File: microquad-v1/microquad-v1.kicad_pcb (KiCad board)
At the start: 2 copper layers, 163.8 x 79.1 mm, 79 parts, among them J1 USB_microB_2040002-1, M1 Motor_DC, M2 Motor_DC, M3 Motor_DC, M4 Motor_DC, M5 Motor_DC, M6 Motor_DC, Q1 Q_NMOS_GSD, Q2 Q_NMOS_GSD, Q3 Q_NMOS_GSD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

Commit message: Merged new netlist
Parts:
- Uimu1: footprint QFN40P300X300X105-25N -> imulogger2:QFN40P300X300X105-25N
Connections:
- C5 pad 2: /Motor6/VBAT -> /Motor1/VBAT
- C6 pad 2: /Motor6/VBAT -> /Motor2/VBAT
- C7 pad 2: /Motor6/VBAT -> /Motor3/VBAT
- C8 pad 2: /Motor6/VBAT -> /Motor4/VBAT
- C9 pad 2: /Motor6/VBAT -> /Motor5/VBAT
- D10 pad 1: Net-(D15-Pad2) -> Net-(D10-Pad1)
- D11 pad 1: /Motor6/VBAT -> /Motor4/VBAT
- D11 pad 2: Net-(D15-Pad2) -> Net-(D11-Pad2)
- D12 pad 1: Net-(D15-Pad2) -> Net-(D11-Pad2)
- D13 pad 1: /Motor6/VBAT -> /Motor5/VBAT
- D13 pad 2: Net-(D15-Pad2) -> Net-(D13-Pad2)
- D14 pad 1: Net-(D15-Pad2) -> Net-(D13-Pad2)
- D5 pad 1: /Motor6/VBAT -> /Motor1/VBAT
- D5 pad 2: Net-(D15-Pad2) -> Net-(D5-Pad2)
- D6 pad 1: Net-(D15-Pad2) -> Net-(D5-Pad2)
- D7 pad 1: /Motor6/VBAT -> /Motor2/VBAT
- D7 pad 2: Net-(D15-Pad2) -> Net-(D7-Pad2)
- D8 pad 1: Net-(D15-Pad2) -> Net-(D7-Pad2)
- D9 pad 1: /Motor6/VBAT -> /Motor3/VBAT
- D9 pad 2: Net-(D15-Pad2) -> Net-(D10-Pad1)
- M1 pad 1: /Motor6/VBAT -> /Motor1/VBAT
- M1 pad 2: Net-(D15-Pad2) -> Net-(D5-Pad2)
- M2 pad 1: /Motor6/VBAT -> /Motor2/VBAT
- M2 pad 2: Net-(D15-Pad2) -> Net-(D7-Pad2)
- M3 pad 1: /Motor6/VBAT -> /Motor3/VBAT
- M3 pad 2: Net-(D15-Pad2) -> Net-(D10-Pad1)
- M4 pad 1: /Motor6/VBAT -> /Motor4/VBAT
- M4 pad 2: Net-(D15-Pad2) -> Net-(D11-Pad2)
- M5 pad 1: /Motor6/VBAT -> /Motor5/VBAT
- M5 pad 2: Net-(D15-Pad2) -> Net-(D13-Pad2)
- Q1 pad 1: /Motor6/ENABLE -> /Motor1/ENABLE
- Q1 pad 3: Net-(D15-Pad2) -> Net-(D5-Pad2)
- Q2 pad 1: /Motor6/ENABLE -> /Motor2/ENABLE
- Q2 pad 3: Net-(D15-Pad2) -> Net-(D7-Pad2)
- Q3 pad 1: /Motor6/ENABLE -> /Motor3/ENABLE
- Q3 pad 3: Net-(D15-Pad2) -> Net-(D10-Pad1)
- Q4 pad 1: /Motor6/ENABLE -> /Motor4/ENABLE
- Q4 pad 3: Net-(D15-Pad2) -> Net-(D11-Pad2)
- Q5 pad 1: /Motor6/ENABLE -> /Motor5/ENABLE
- Q5 pad 3: Net-(D15-Pad2) -> Net-(D13-Pad2)

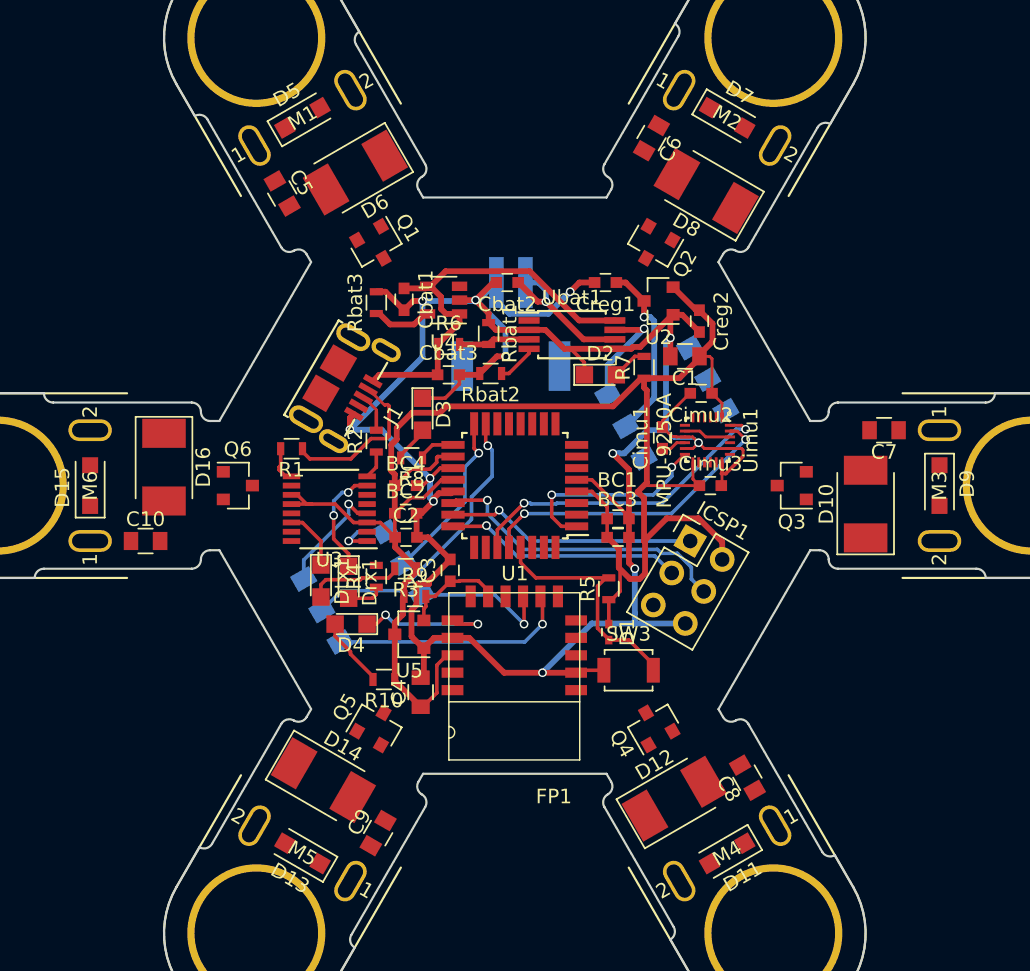
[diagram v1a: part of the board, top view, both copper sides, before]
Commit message: Add tracks on arms and connect VBAT, requires DRC violations... (not actual violations, KiCad just thinks they are)
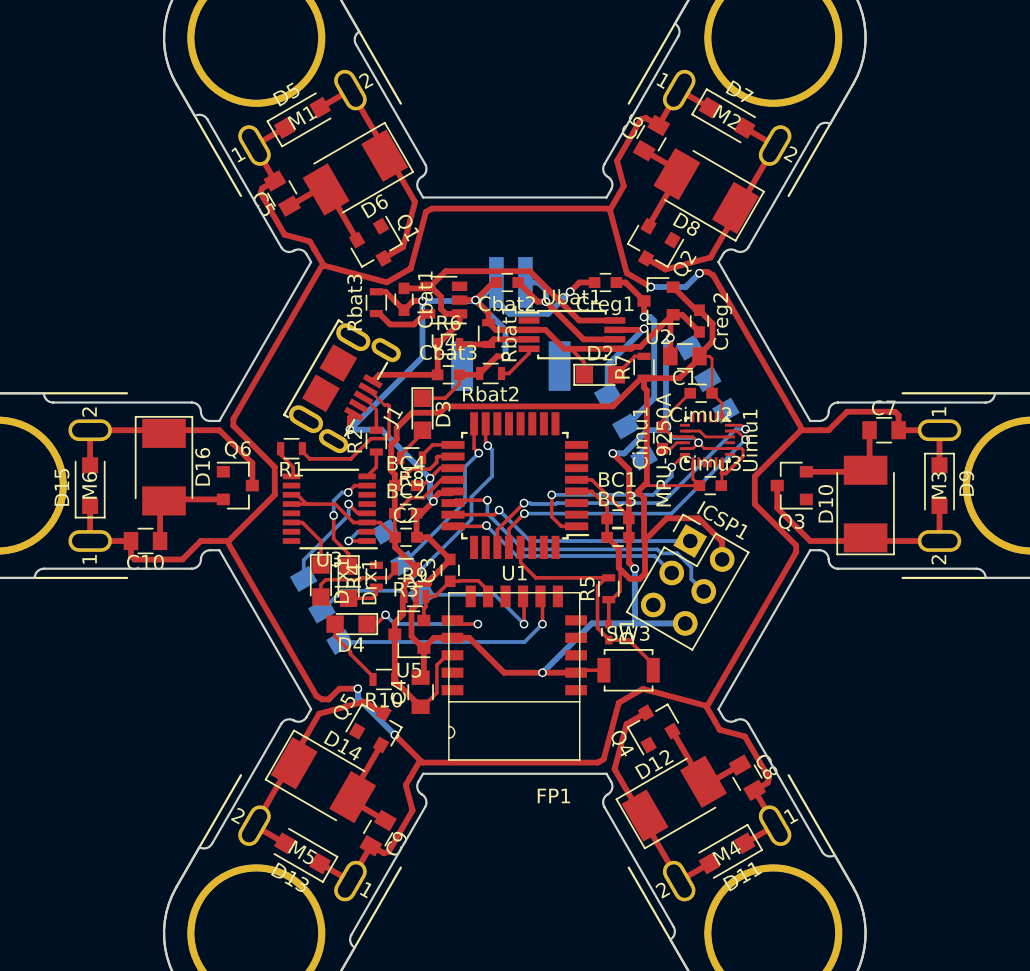
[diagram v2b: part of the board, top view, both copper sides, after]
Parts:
- turned C10 to 180 degrees
- turned C5 to 120 degrees
- turned C6 to 60 degrees
- turned C7 to 0 degrees
- turned C8 to 300 degrees
- turned C9 to 240 degrees
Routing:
- net /Motor4/VBAT: track 0.00 -> 58.9 mm, vias 0 -> 2
- net GND: track 170.6 -> 209.9 mm
- net /Motor2/VBAT: track 0.00 -> 36.8 mm, vias 0 -> 2
- net /Motor6/VBAT: track 0.00 -> 36.7 mm
- net /Motor1/VBAT: track 0.00 -> 36.5 mm
- net /Motor3/VBAT: track 0.00 -> 36.5 mm
- net Net-(D15-Pad2): track 0.00 -> 16.4 mm
- net /Motor5/VBAT: track 0.00 -> 13.6 mm
- net Net-(D7-Pad2): track 0.00 -> 13.5 mm
- net Net-(D13-Pad2): track 0.00 -> 13.5 mm
- net Net-(D10-Pad1): track 0.00 -> 13.5 mm
- net Net-(D5-Pad2): track 0.00 -> 13.5 mm
- net Net-(D11-Pad2): track 0.00 -> 13.5 mm

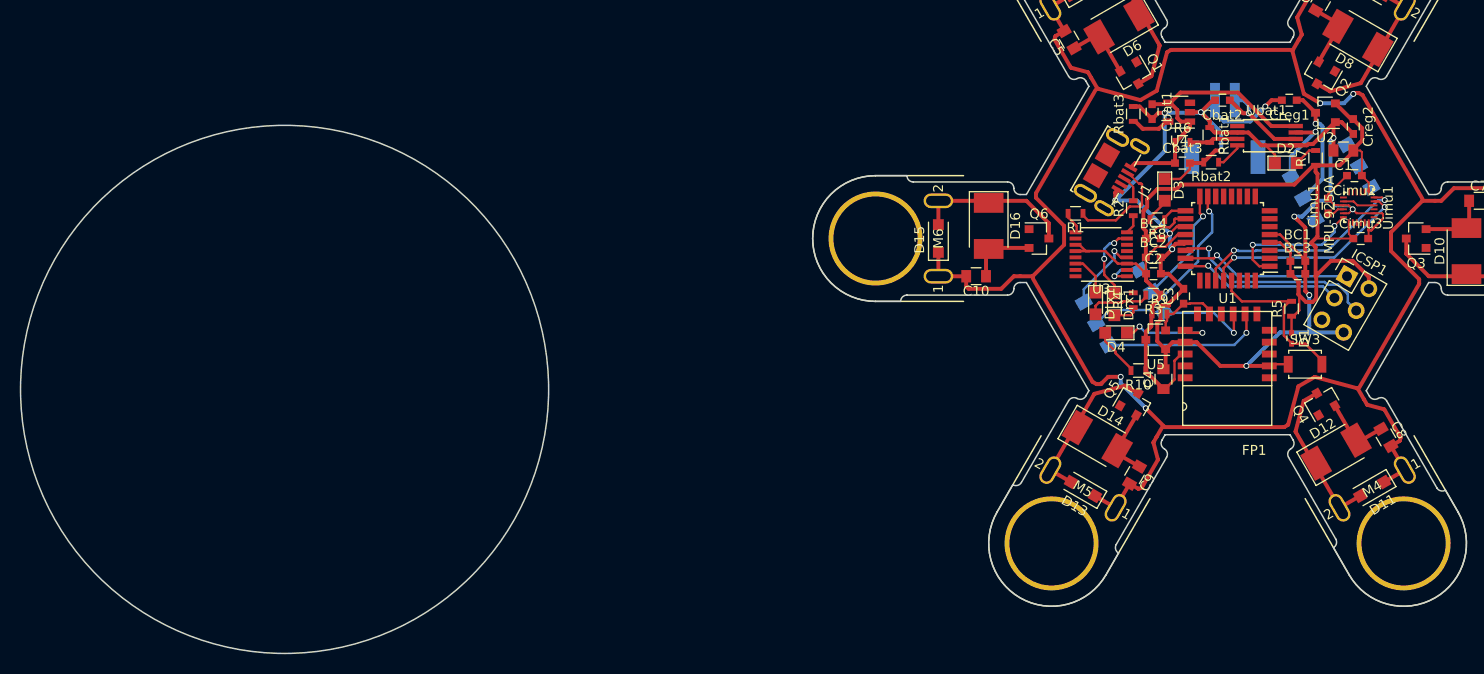
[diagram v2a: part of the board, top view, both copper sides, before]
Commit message: Fixed VBAT connections
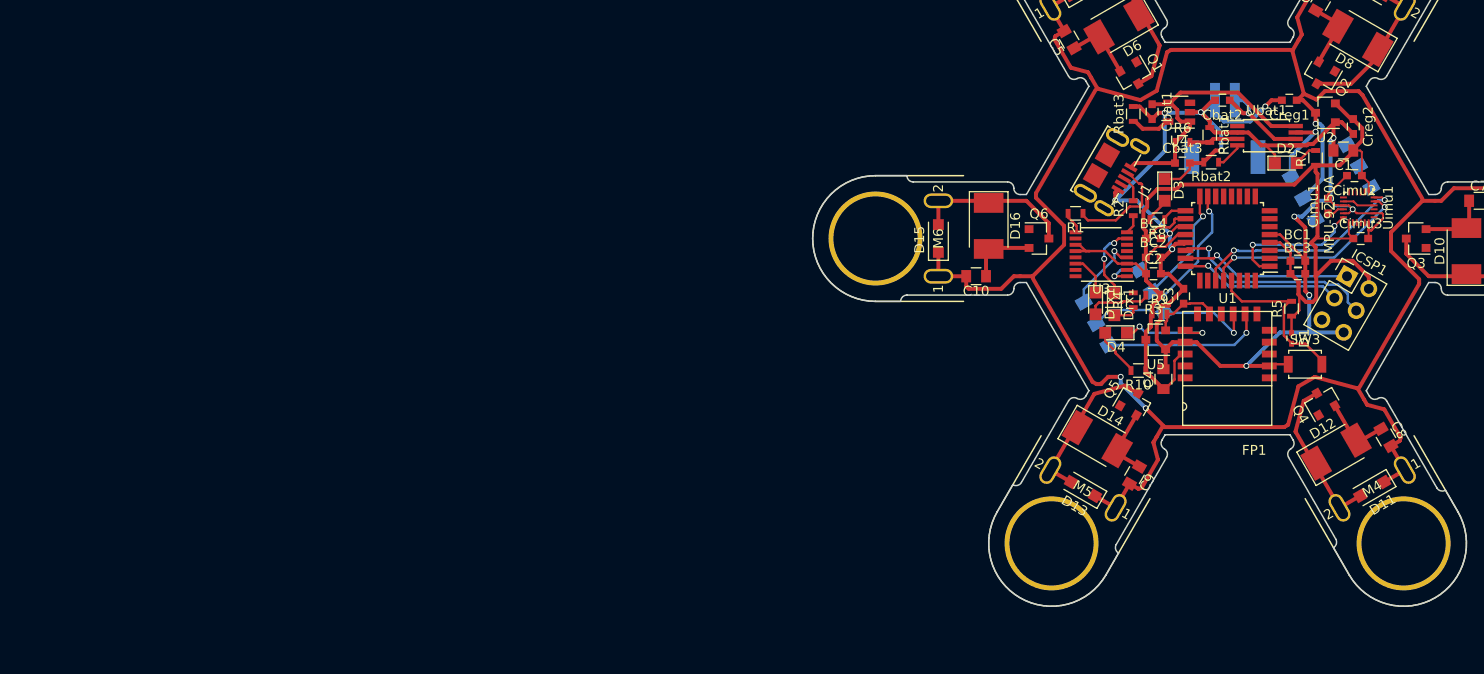
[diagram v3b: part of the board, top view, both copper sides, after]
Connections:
- C10 pad 2: /Motor6/VBAT -> /VBAT
- C5 pad 2: /Motor1/VBAT -> /VBAT
- C6 pad 2: /Motor2/VBAT -> /VBAT
- C7 pad 2: /Motor3/VBAT -> /VBAT
- C8 pad 2: /Motor4/VBAT -> /VBAT
- C9 pad 2: /Motor5/VBAT -> /VBAT
- D11 pad 1: /Motor4/VBAT -> /VBAT
- D13 pad 1: /Motor5/VBAT -> /VBAT
- D15 pad 1: /Motor6/VBAT -> /VBAT
- D5 pad 1: /Motor1/VBAT -> /VBAT
- D7 pad 1: /Motor2/VBAT -> /VBAT
- D9 pad 1: /Motor3/VBAT -> /VBAT
- M1 pad 1: /Motor1/VBAT -> /VBAT
- M2 pad 1: /Motor2/VBAT -> /VBAT
- M3 pad 1: /Motor3/VBAT -> /VBAT
- M4 pad 1: /Motor4/VBAT -> /VBAT
- M5 pad 1: /Motor5/VBAT -> /VBAT
- M6 pad 1: /Motor6/VBAT -> /VBAT
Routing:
- net /VBAT: track 12.4 -> 232.4 mm, vias 1 -> 3
- net /Motor4/VBAT: track 58.9 -> 0.00 mm, vias 2 -> 0
- net /Motor2/VBAT: track 36.8 -> 0.00 mm, vias 2 -> 0
- net /Motor6/VBAT: track 36.7 -> 0.00 mm
- net /Motor1/VBAT: track 36.5 -> 0.00 mm
- net /Motor3/VBAT: track 36.5 -> 0.00 mm
- net /Motor5/VBAT: track 13.6 -> 0.00 mm
- net Net-(D7-Pad2): track 13.5 -> 12.9 mm
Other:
- board size 163.8 x 79.1 mm -> 83.8 x 74.3 mm

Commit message: Fixed disconnects around the board
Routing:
- net GND: track 210.0 -> 229.0 mm, vias 12 -> 20
- net +3V3: track 127.6 -> 137.7 mm
- net Net-(Cbat2-Pad1): track 10.7 -> 15.5 mm
- net /RESET: track 16.7 -> 20.8 mm
- net /VBAT: track 232.4 -> 234.5 mm, vias 3 -> 1
- net /IMU/SDA: track 22.4 -> 23.7 mm
- net /IMU/SCL: track 21.7 -> 22.5 mm
- net Net-(D13-Pad2): track 13.5 -> 12.9 mm
- net /USB interface/5V: track 29.6 -> 30.1 mm
- added copper zone on B.Cu, net GND

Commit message: Ladybug is satisfied
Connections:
- U1 pad 13: /Motor5/ENABLE -> /Motor2/ENABLE
- U1 pad 14: /Motor4/ENABLE -> /Motor1/ENABLE
- U1 pad 31: /Motor2/ENABLE -> /Motor5/ENABLE
- U1 pad 32: /Motor1/ENABLE -> /Motor4/ENABLE
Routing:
- net /Motor1/ENABLE: track 0.00 -> 37.0 mm, vias 0 -> 2
- net /Motor2/ENABLE: track 0.00 -> 35.8 mm, vias 0 -> 2
- net /Motor5/ENABLE: track 0.00 -> 33.7 mm, vias 0 -> 2
- net GND: track 229.0 -> 261.5 mm, vias 20 -> 25
- net /Motor6/ENABLE: track 0.00 -> 28.3 mm, vias 0 -> 2
- net /Motor3/ENABLE: track 0.00 -> 25.1 mm, vias 0 -> 2
- net /Motor4/ENABLE: track 0.00 -> 23.5 mm, vias 0 -> 2
- net /VBAT: track 234.5 -> 237.6 mm
- net /IMU_INT: track 14.2 -> 13.4 mm
- net +3V3: track 137.7 -> 138.4 mm

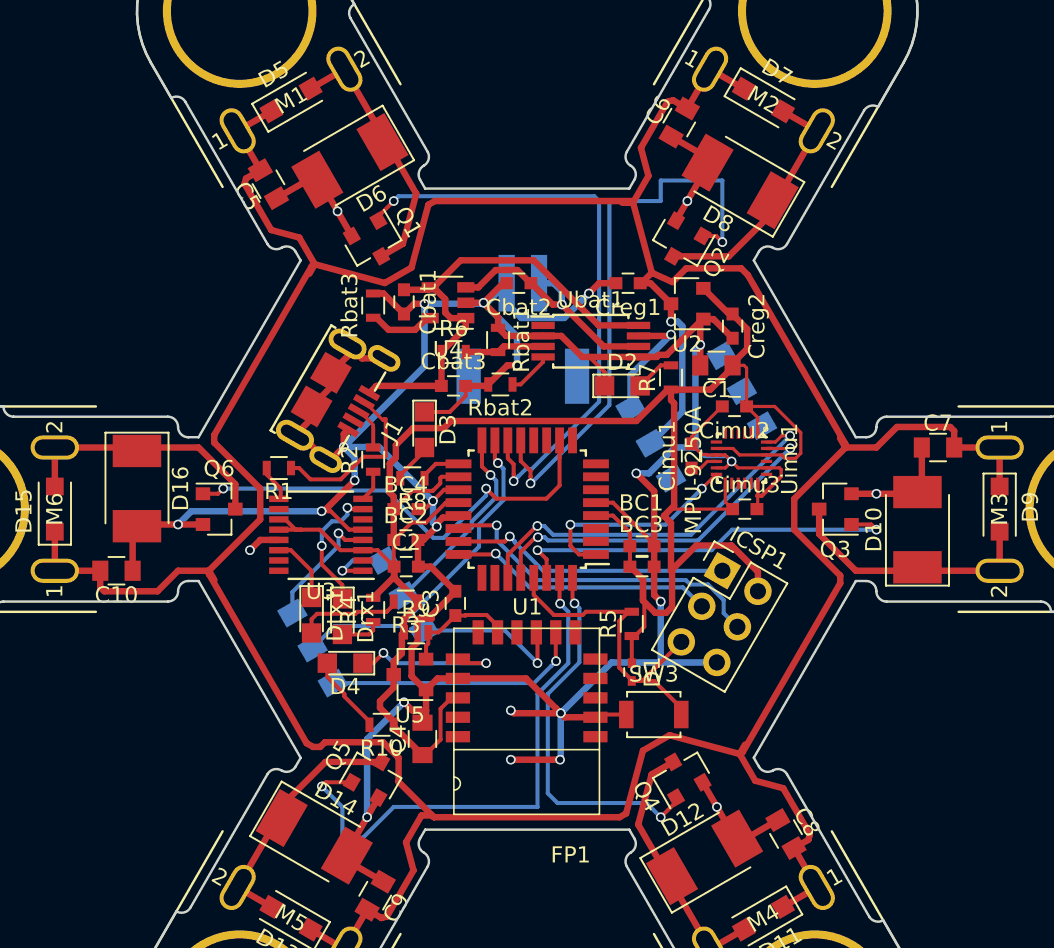
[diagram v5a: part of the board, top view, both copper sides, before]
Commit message: Better bridges
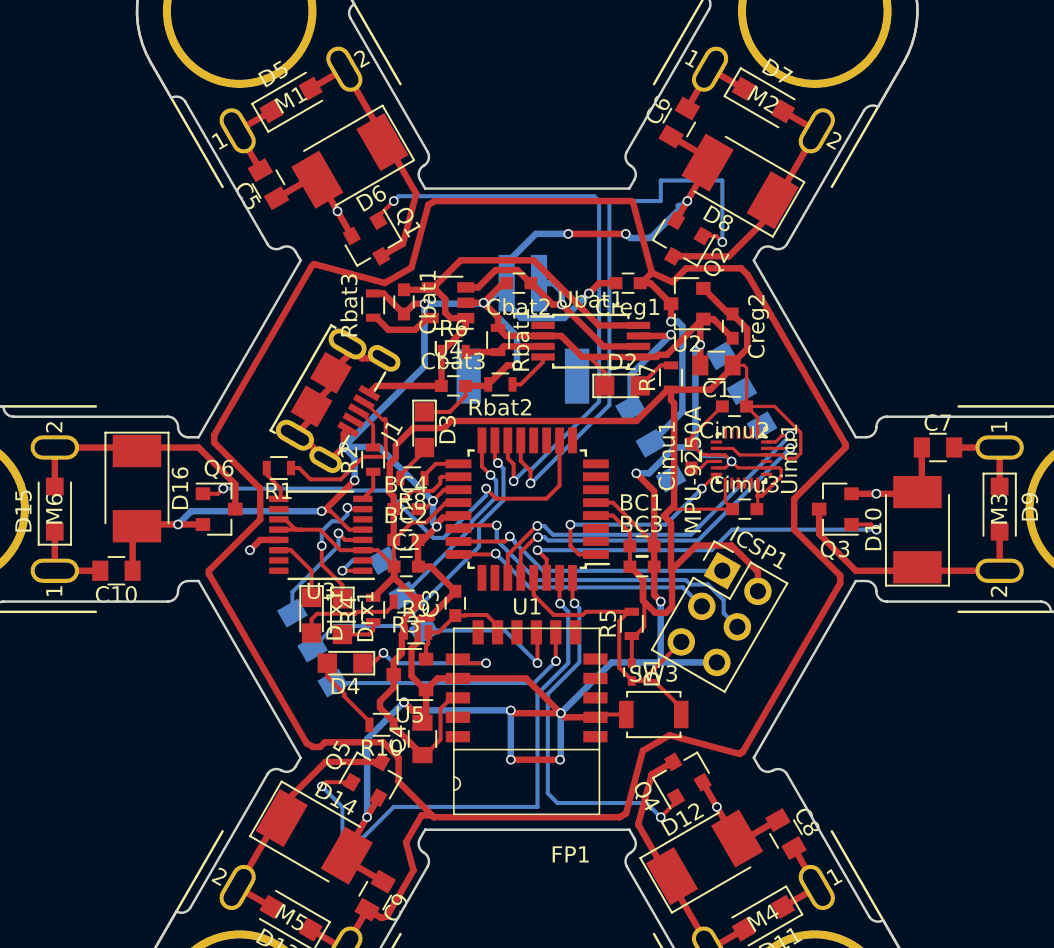
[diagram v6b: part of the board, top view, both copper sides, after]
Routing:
- net /VBAT: track 237.6 -> 192.4 mm
- net GND: track 261.5 -> 286.2 mm, vias 25 -> 27
